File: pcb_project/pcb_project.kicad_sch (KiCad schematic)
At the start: 15 parts, among them J6 Conn_01x10_Pin

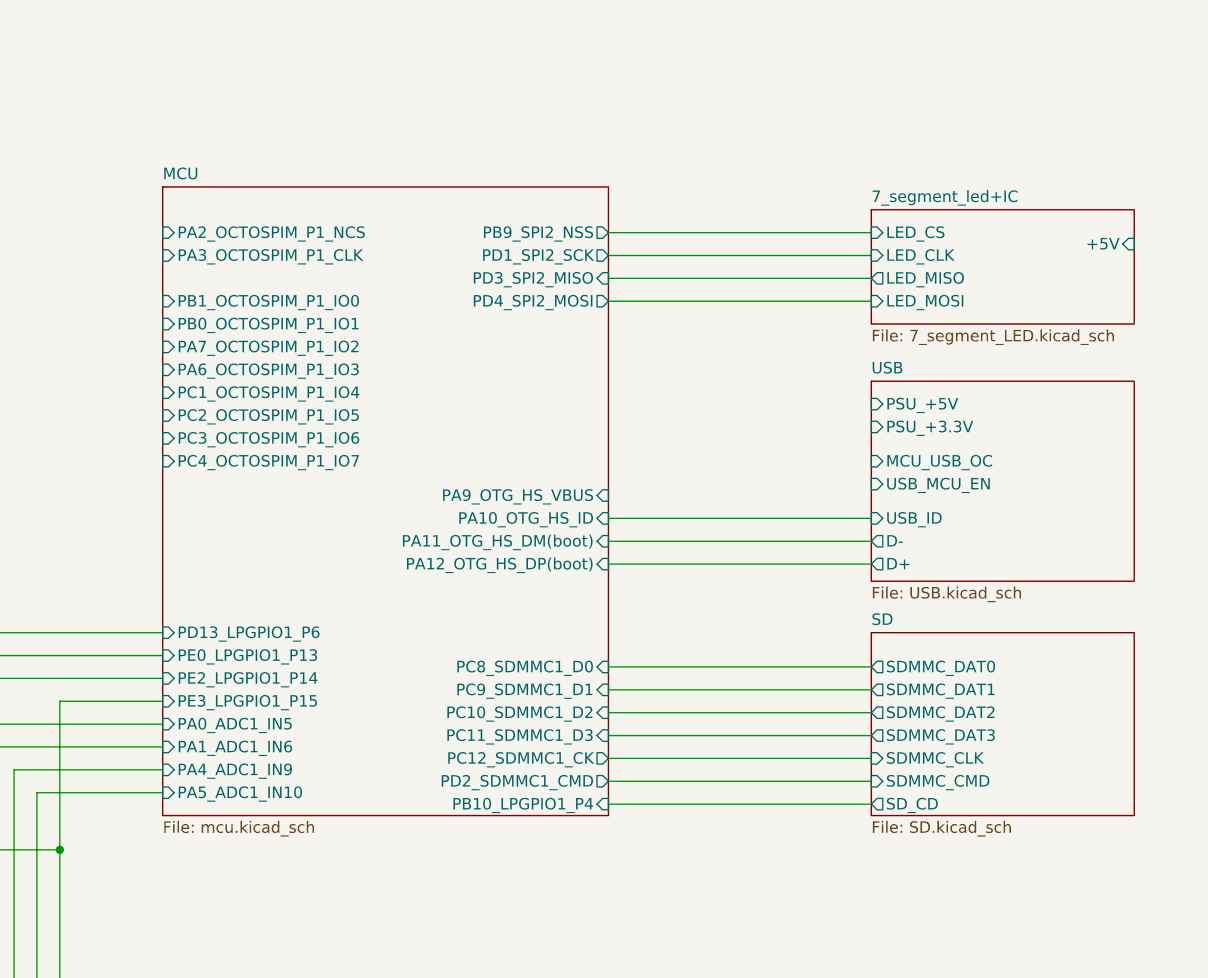
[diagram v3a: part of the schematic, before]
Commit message: Update USB component and redo pin choices for MCU
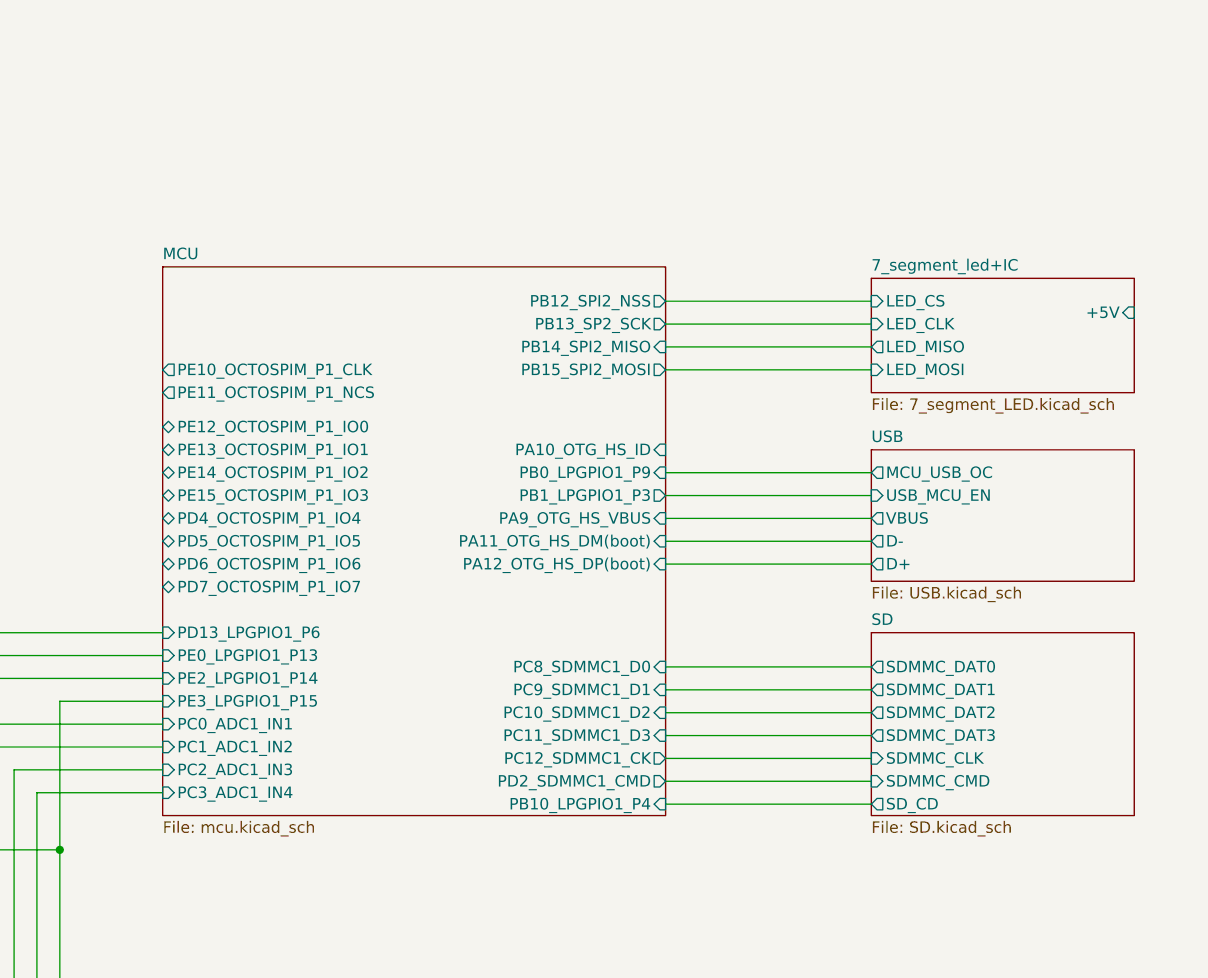
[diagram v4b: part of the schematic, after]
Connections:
- net MCU/PA0_ADC1_IN5 renamed MCU/PC0_ADC1_IN1
- net MCU/PA1_ADC1_IN6 renamed MCU/PC1_ADC1_IN2
- net MCU/PA4_ADC1_IN9 renamed MCU/PC2_ADC1_IN3
- net MCU/PA5_ADC1_IN10 renamed MCU/PC3_ADC1_IN4
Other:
- sheet MCU ports: added PB0_LPGPIO1_P9, PB12_SPI2_NSS, PB13_SP2_SCK, PB14_SPI2_MISO, PB15_SPI2_MOSI, PB1_LPGPIO1_P3, PC0_ADC1_IN1, PC1_ADC1_IN2, PC2_ADC1_IN3, PC3_ADC1_IN4, PD4_OCTOSPIM_P1_IO4, PD5_OCTOSPIM_P1_IO5, PD6_OCTOSPIM_P1_IO6, PD7_OCTOSPIM_P1_IO7, PE10_OCTOSPIM_P1_CLK, PE11_OCTOSPIM_P1_NCS, PE12_OCTOSPIM_P1_IO0, PE13_OCTOSPIM_P1_IO1, PE14_OCTOSPIM_P1_IO2, PE15_OCTOSPIM_P1_IO3; removed PA0_ADC1_IN5, PA1_ADC1_IN6, PA2_OCTOSPIM_P1_NCS, PA3_OCTOSPIM_P1_CLK, PA4_ADC1_IN9, PA5_ADC1_IN10, PA6_OCTOSPIM_P1_IO3, PA7_OCTOSPIM_P1_IO2, PB0_OCTOSPIM_P1_IO1, PB1_OCTOSPIM_P1_IO0, PB9_SPI2_NSS, PC1_OCTOSPIM_P1_IO4, PC2_OCTOSPIM_P1_IO5, PC3_OCTOSPIM_P1_IO6, PC4_OCTOSPIM_P1_IO7, PD1_SPI2_SCK, PD3_SPI2_MISO, PD4_SPI2_MOSI
- sheet USB ports: added VBUS; removed PSU_+3.3V, PSU_+5V, USB_ID

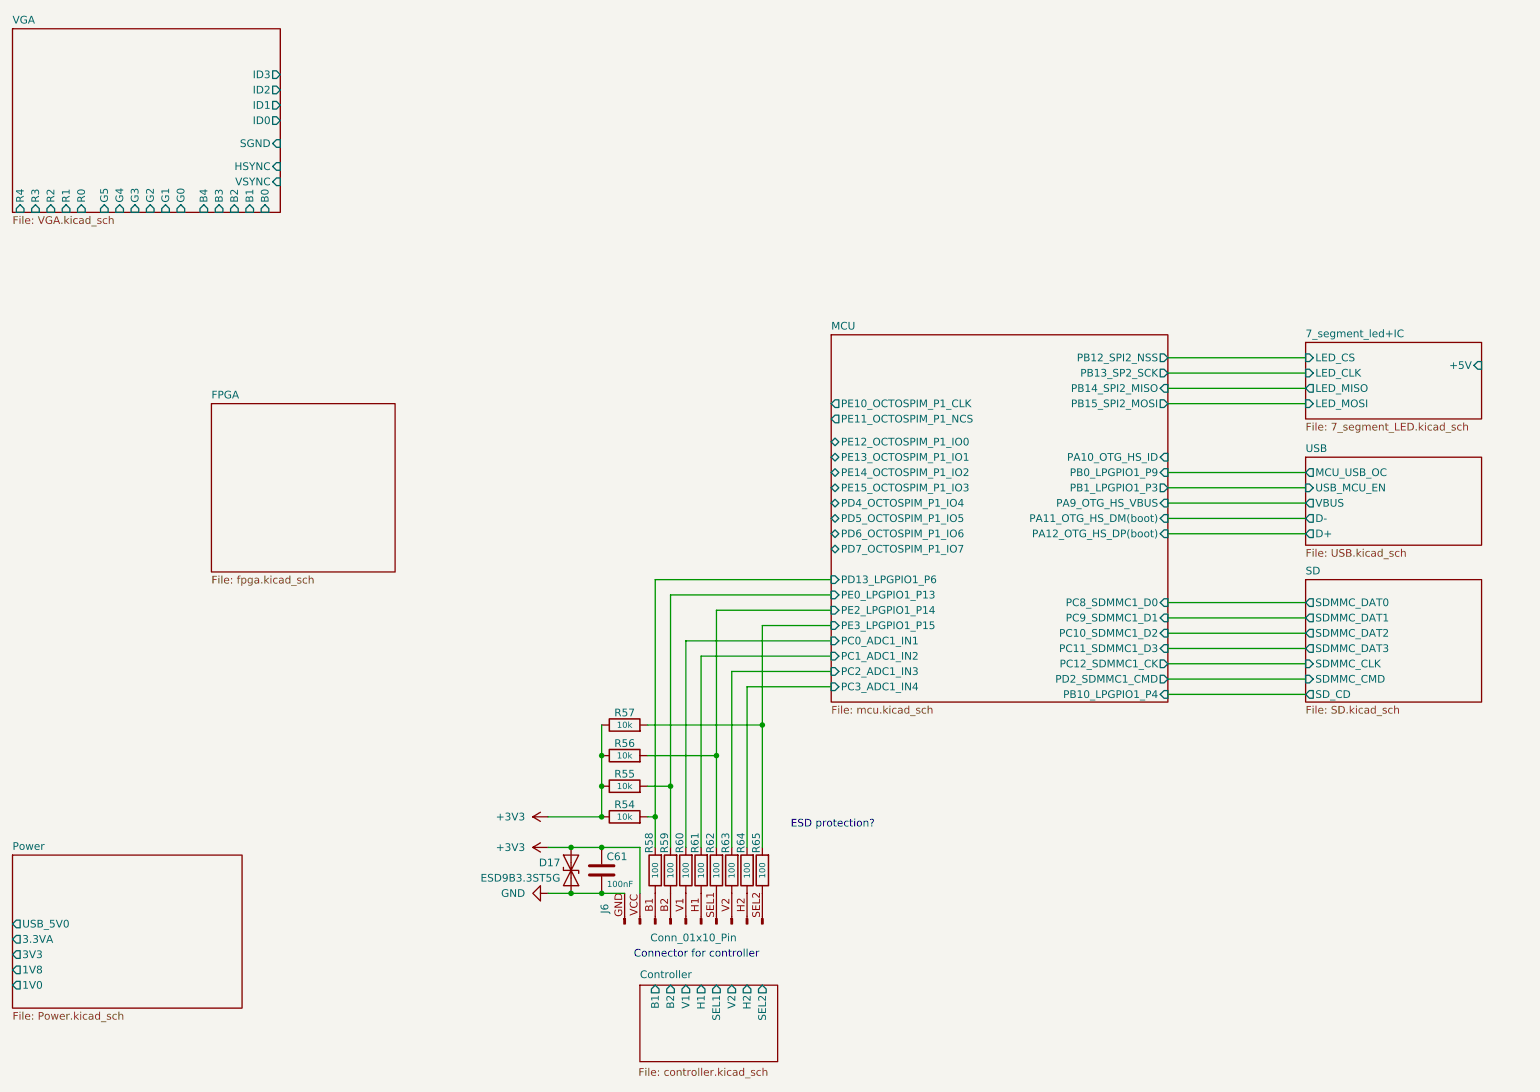
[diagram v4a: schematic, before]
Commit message: SPI connection root
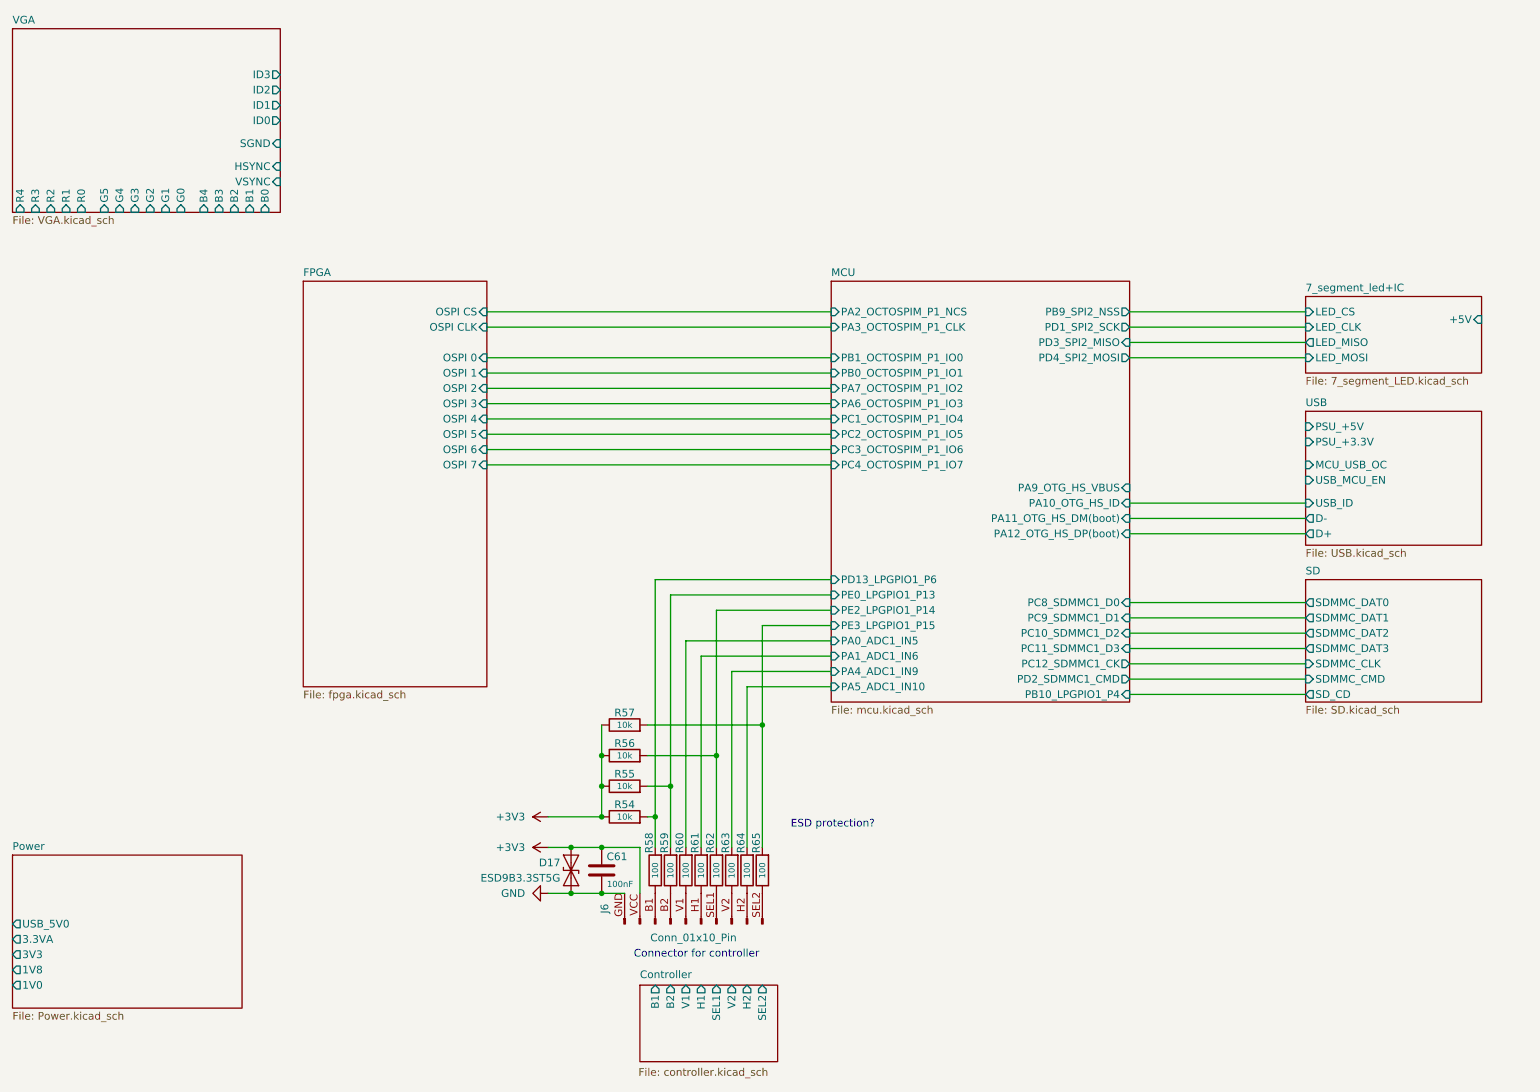
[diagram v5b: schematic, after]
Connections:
- net MCU/PC0_ADC1_IN1 renamed MCU/PA0_ADC1_IN5
- net MCU/PC1_ADC1_IN2 renamed MCU/PA1_ADC1_IN6
- net MCU/PC2_ADC1_IN3 renamed MCU/PA4_ADC1_IN9
- net MCU/PC3_ADC1_IN4 renamed MCU/PA5_ADC1_IN10
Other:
- sheet FPGA ports: added OSPI 0, OSPI 1, OSPI 2, OSPI 3, OSPI 4, OSPI 5, OSPI 6, OSPI 7, OSPI CLK, OSPI CS; removed none
- sheet MCU ports: added PA0_ADC1_IN5, PA1_ADC1_IN6, PA2_OCTOSPIM_P1_NCS, PA3_OCTOSPIM_P1_CLK, PA4_ADC1_IN9, PA5_ADC1_IN10, PA6_OCTOSPIM_P1_IO3, PA7_OCTOSPIM_P1_IO2, PB0_OCTOSPIM_P1_IO1, PB1_OCTOSPIM_P1_IO0, PB9_SPI2_NSS, PC1_OCTOSPIM_P1_IO4, PC2_OCTOSPIM_P1_IO5, PC3_OCTOSPIM_P1_IO6, PC4_OCTOSPIM_P1_IO7, PD1_SPI2_SCK, PD3_SPI2_MISO, PD4_SPI2_MOSI; removed PB0_LPGPIO1_P9, PB12_SPI2_NSS, PB13_SP2_SCK, PB14_SPI2_MISO, PB15_SPI2_MOSI, PB1_LPGPIO1_P3, PC0_ADC1_IN1, PC1_ADC1_IN2, PC2_ADC1_IN3, PC3_ADC1_IN4, PD4_OCTOSPIM_P1_IO4, PD5_OCTOSPIM_P1_IO5, PD6_OCTOSPIM_P1_IO6, PD7_OCTOSPIM_P1_IO7, PE10_OCTOSPIM_P1_CLK, PE11_OCTOSPIM_P1_NCS, PE12_OCTOSPIM_P1_IO0, PE13_OCTOSPIM_P1_IO1, PE14_OCTOSPIM_P1_IO2, PE15_OCTOSPIM_P1_IO3
- sheet USB ports: added PSU_+3.3V, PSU_+5V, USB_ID; removed VBUS

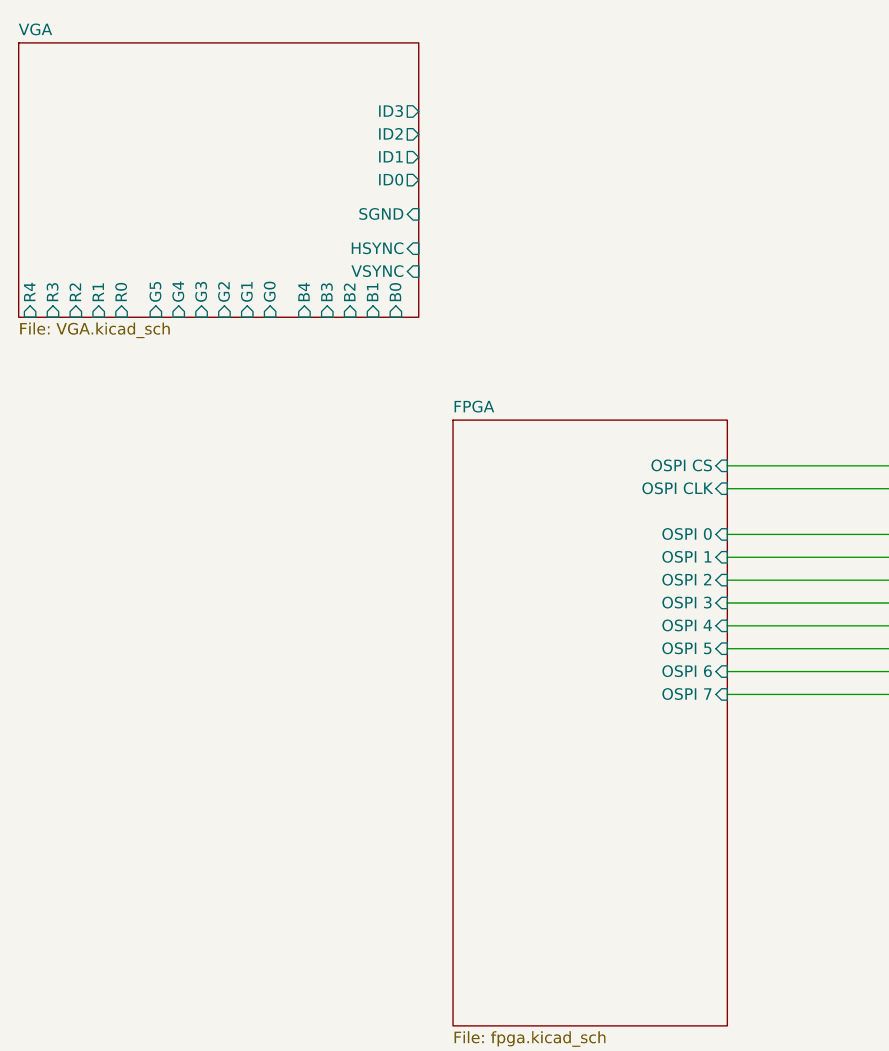
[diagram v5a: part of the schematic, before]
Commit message: VGA Root + Change FPGA Oscilator to 3.3v
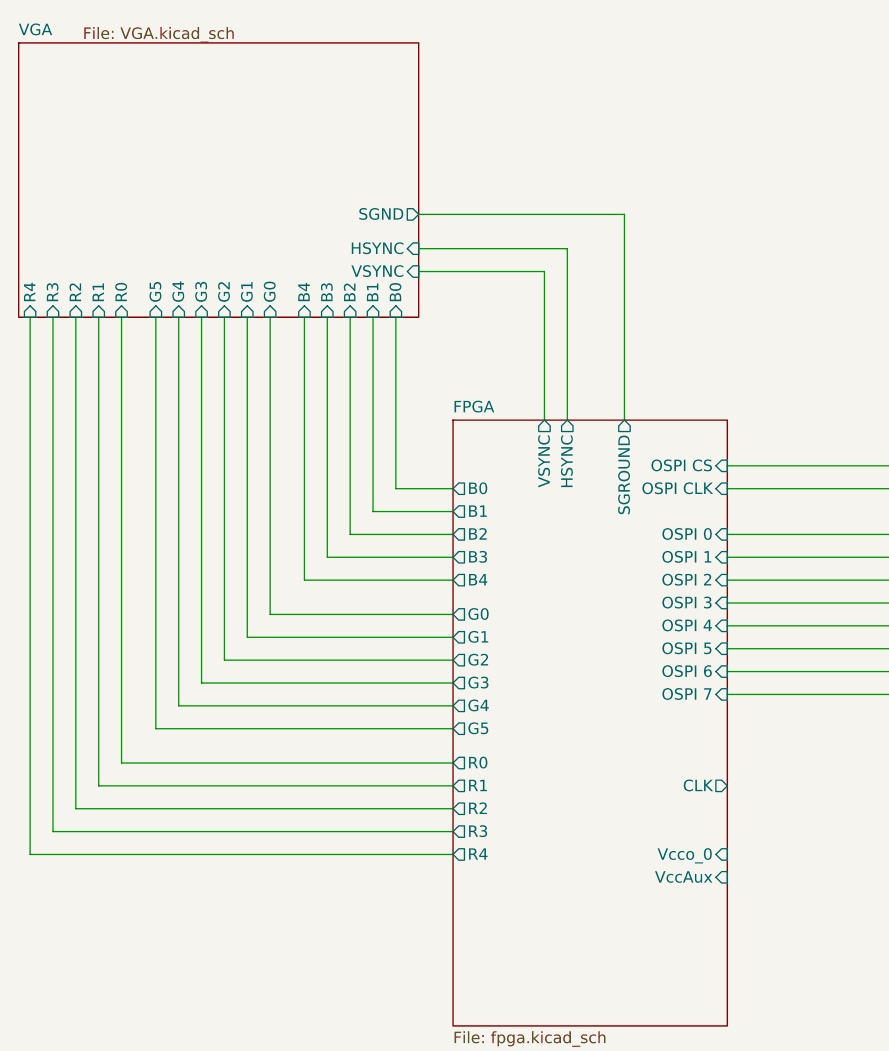
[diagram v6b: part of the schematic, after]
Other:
- sheet FPGA ports: added B0, B1, B2, B3, B4, CLK, G0, G1, G2, G3, G4, G5, HSYNC, R0, R1, R2, R3, R4, SGROUND, VSYNC, VccAux, Vcco_0; removed none
- sheet VGA ports: added none; removed ID0, ID1, ID2, ID3

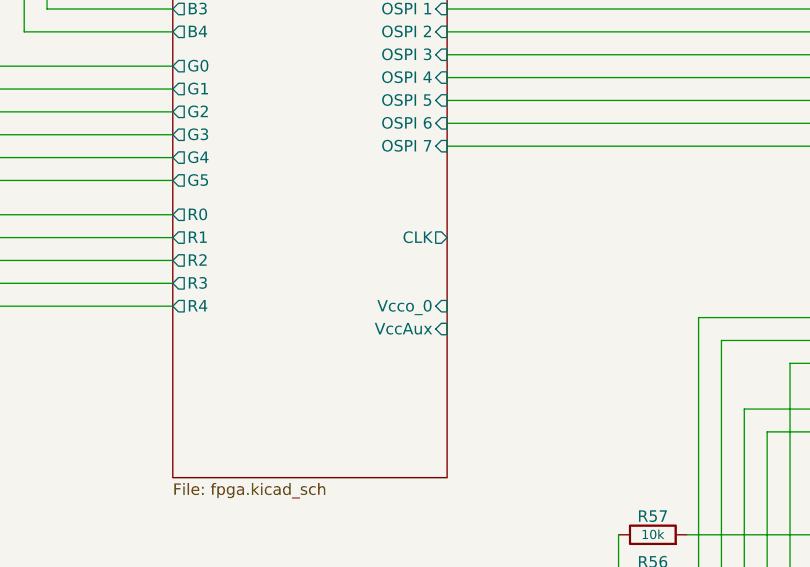
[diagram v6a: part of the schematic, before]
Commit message: Remove unused inputs to FPGA in root
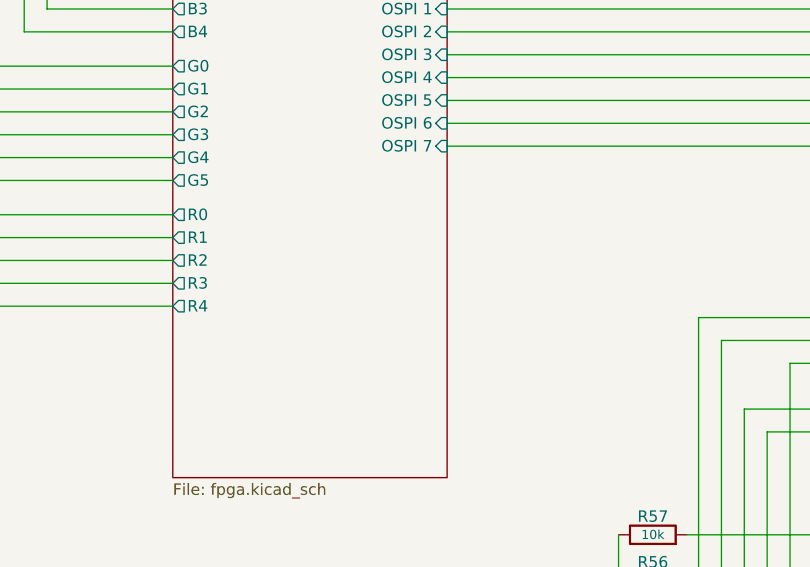
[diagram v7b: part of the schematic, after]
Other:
- sheet FPGA ports: added none; removed CLK, VccAux, Vcco_0
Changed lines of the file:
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@@
-			)
-		)
-		(pin "CLK" output
-			(at 104.14 105.41 0)
-			(effects
-				(font
-					(size 1.27 1.27)
-				)
-				(justify right)
 			)
 		)
@@
 			(effects
 				(font
-					(size 1.27 1.27)
-				)
-				(justify right)
-			)
-		)
-		(pin "VccAux" input
-			(at 104.14 115.57 0)
-			(effects
-				(font
-					(size 1.27 1.27)
-				)
-				(justify right)
-			)
-		)
-		(pin "Vcco_0" input
-			(at 104.14 113.03 0)
-			(effects
-				(font
